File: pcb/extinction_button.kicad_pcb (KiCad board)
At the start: 2 copper layers, 47.8 x 61.3 mm, 36 parts, among them J1 DX07S016JA1R1500, J2 Conn_01x02, J3 Conn_01x06, SW1 R-667843, U1 ATmega32U4-A, U2 MIC5219-5.0YM5, Y1 ECS-160-10-36-CKM-TR3

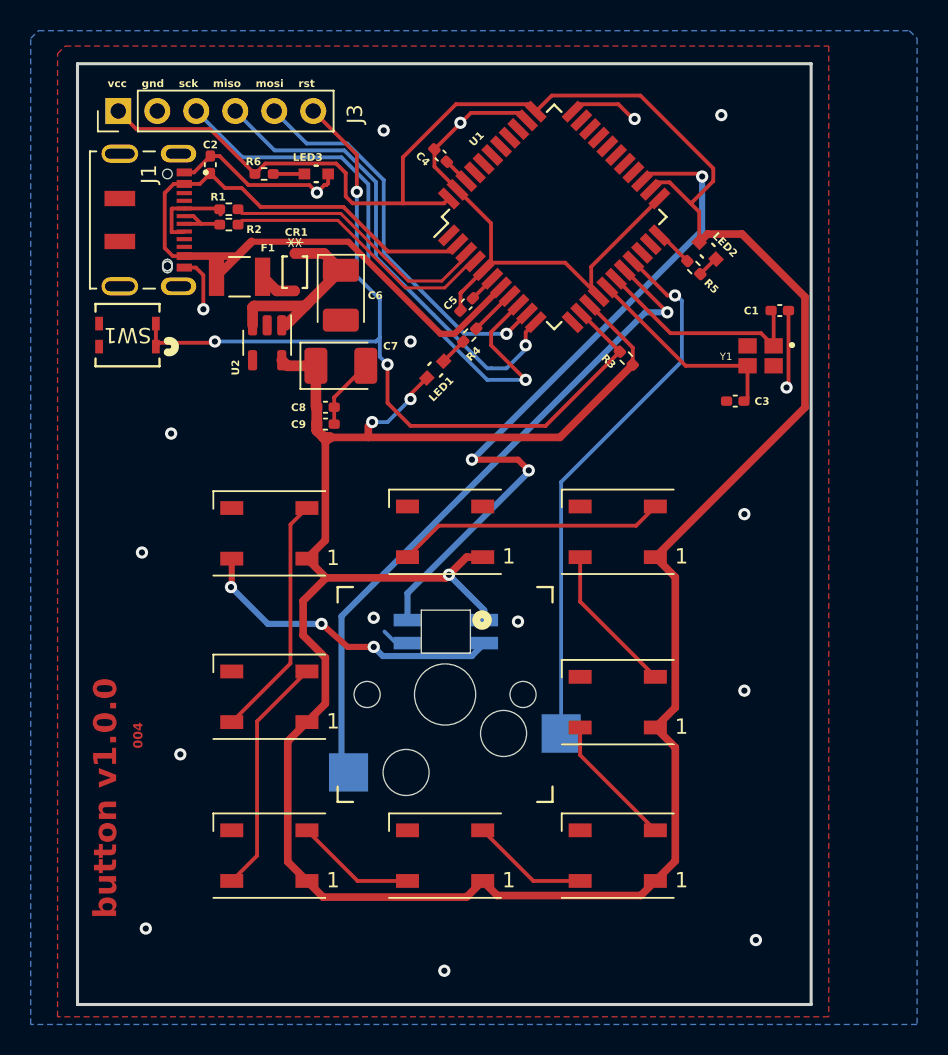
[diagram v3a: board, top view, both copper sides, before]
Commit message: re-add mounting holes
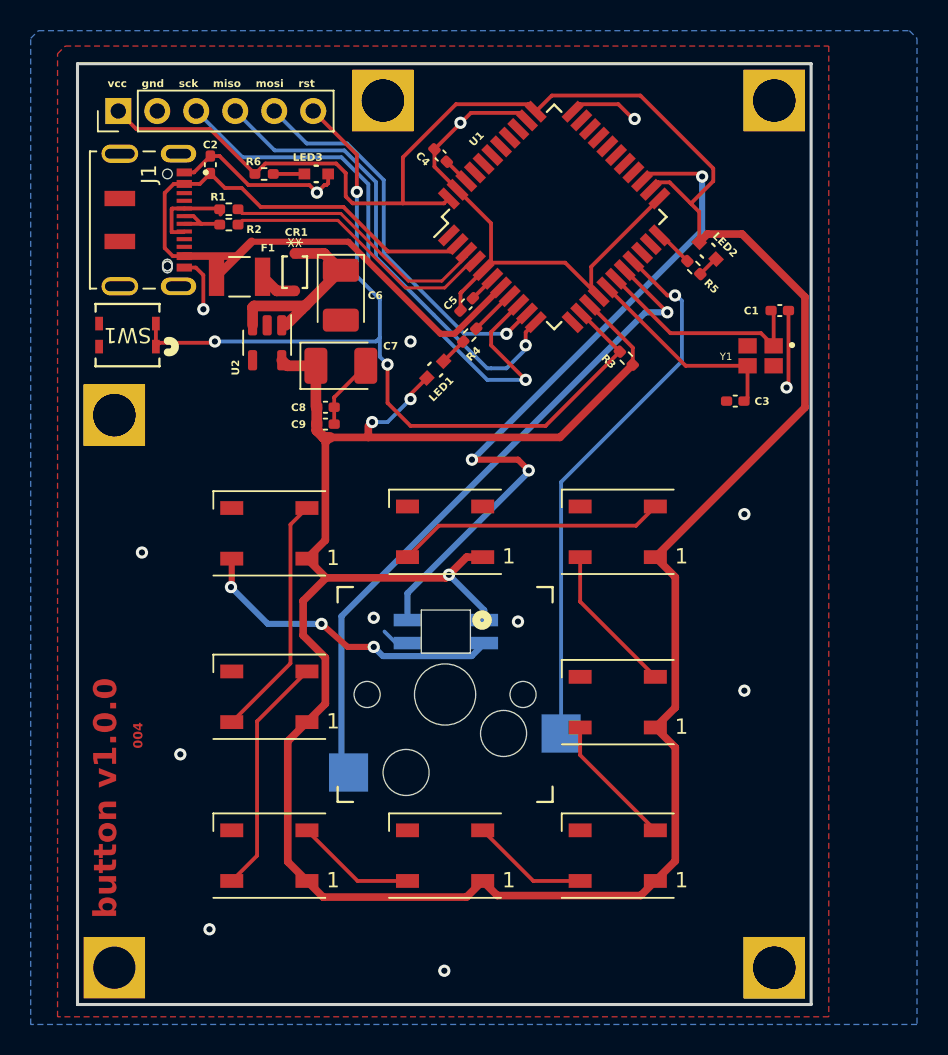
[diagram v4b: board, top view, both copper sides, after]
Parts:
- added ?: , , F.Cu at (196.2, 49.3)
- added ?: , clipboard:4f5b61f9-1e4c-4a2e-b6b5-7684ae1e77c1, F.Cu at (221.7, 105.8)
- added ?: , , F.Cu at (178.7, 69.8)
- added ?: , , F.Cu at (221.7, 49.3)
- added ?: , clipboard:4f5b61f9-1e4c-4a2e-b6b5-7684ae1e77c1, F.Cu at (196.2, 49.3)
- added ?: , clipboard:4f5b61f9-1e4c-4a2e-b6b5-7684ae1e77c1, F.Cu at (178.7, 69.8)
- added ?: , , F.Cu at (221.7, 105.8)
- added ?: , clipboard:4f5b61f9-1e4c-4a2e-b6b5-7684ae1e77c1, F.Cu at (178.7, 105.8)
- added ?: , clipboard:4f5b61f9-1e4c-4a2e-b6b5-7684ae1e77c1, F.Cu at (221.7, 49.3)
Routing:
- net GND: vias 18 -> 14
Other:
- board text removed: "JLCJLCJLCJLC"
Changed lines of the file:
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@@
     )
   )
+  (footprint "" (layer "F.Cu")
+    (at 196.2 49.3)
+    (fp_text reference "" (at 0 0) (layer "F.SilkS")
+        (effects (font (size 1.27 1.27) (thickness 0.15)))
+    )
+    (fp_text value "" (at 0 0) (layer "F.SilkS")
+        (effects (font (size 1.27 1.27) (thickness 0.15)))
+    )
+    (pad "1" thru_hole rect (at 0 0) (size 4 4) (drill 2.75) (layers "*.Cu" "*.Mask")
+      (net 1 "GND"))
+  )
   (footprint "Capacitor_SMD:C_0402_1005Metric_Pad0.74x0.62mm_HandSolder" (layer "F.Cu")
     (at 192.45706 69.283704)
@@
     )
   )
+  (footprint "clipboard:4f5b61f9-1e4c-4a2e-b6b5-7684ae1e77c1" (layer "F.Cu")
+    (at 221.7 105.8)
+    (fp_text reference "" (at 0 0) (layer "F.SilkS")
+        (effects (font (size 1.27 1.27) (thickness 0.15)))
+    )
+    (fp_text value "" (at 0 0) (layer "F.SilkS")
+        (effects (font (size 1.27 1.27) (thickness 0.15)))
+    )
+    (pad "1" thru_hole rect (at 0 0) (size 4 4) (drill 2.75) (layers "*.Cu" "*.Mask")
+      (net 1 "GND"))
+  )
   (footprint "Capacitor_Tantalum_SMD:CP_EIA-3528-15_AVX-H_Pad1.50x2.35mm_HandSolder" (layer "F.Cu")
     (at 193.45706 66.583704)
@@
     )
   )
+  (footprint "" (layer "F.Cu")
+    (at 178.7 69.8)
+    (fp_text reference "" (at 0 0) (layer "F.SilkS")
+        (effects (font (size 1.27 1.27) (thickness 0.15)))
+    )
+    (fp_text value "" (at 0 0) (layer "F.SilkS")
+        (effects (font (size 1.27 1.27) (thickness 0.15)))
+    )
+    (pad "1" thru_hole rect (at 0 0) (size 4 4) (drill 2.75) (layers "*.Cu" "*.Mask")
+      (net 1 "GND"))
+  )
   (footprint "LED_SMD:LED_WS2812B_PLCC4_5.0x5.0mm_P3.2mm" (layer "F.Cu")
     (at 211.5 77.4 180)
@@
     )
   )
+  (footprint "" (layer "F.Cu")
+    (at 221.7 49.3)
+    (fp_text reference "" (at 0 0) (layer "F.SilkS")
+        (effects (font (size 1.27 1.27) (thickness 0.15)))
+    )
+    (fp_text value "" (at 0 0) (layer "F.SilkS")
+        (effects (font (size 1.27 1.27) (thickness 0.15)))
+    )
+    (pad "1" thru_hole rect (at 0 0) (size 4 4) (drill 2.75) (layers "*.Cu" "*.Mask")
+      (net 1 "GND"))
+  )
   (footprint "Resistor_SMD:R_0402_1005Metric_Pad0.72x0.64mm_HandSolder" (layer "F.Cu")
     (at 188.45706 54.083704)
@@
     )
   )
+  (footprint "clipboard:4f5b61f9-1e4c-4a2e-b6b5-7684ae1e77c1" (layer "F.Cu")
+    (at 196.2 49.3)
+    (fp_text reference "" (at 0 0) (layer "F.SilkS")
+        (effects (font (size 1.27 1.27) (thickness 0.15)))
+    )
+    (fp_text value "" (at 0 0) (layer "F.SilkS")
+        (effects (font (size 1.27 1.27) (thickness 0.15)))
+    )
+    (pad "1" thru_hole rect (at 0 0) (size 4 4) (drill 2.75) (layers "*.Cu" "*.Mask")
+      (net 1 "GND"))
+  )
   (footprint "Connector_PinHeader_2.54mm:PinHeader_1x06_P2.54mm_Vertical" (layer "F.Cu")
     (at 178.95706 49.983704 90)
@@
     (property "ki_keywords" "connector")
     (attr through_hole)
-    (fp_text reference "J3" (at -0.2 15.42 90) (layer "F.SilkS")
+    (fp_text reference "J3" (at -0.2 15.42 90) (layer "F.SilkS") hide
         (effects (font (size 1 1) (thickness 0.15)))
     )
@@
     )
   )
+  (footprint "clipboard:4f5b61f9-1e4c-4a2e-b6b5-7684ae1e77c1" (layer "F.Cu")
+    (at 178.7 69.8)
+    (fp_text reference "" (at 0 0) (layer "F.SilkS")
+        (effects (font (size 1.27 1.27) (thickness 0.15)))
+    )
+    (fp_text value "" (at 0 0) (layer "F.SilkS")
+        (effects (font (size 1.27 1.27) (thickness 0.15)))
+    )
+    (pad "1" thru_hole rect (at 0 0) (size 4 4) (drill 2.75) (layers "*.Cu" "*.Mask")
+      (net 1 "GND"))
+  )
   (footprint "footprints:LED_LTST-C191KRKT_LTO" (layer "F.Cu")
     (at 191.85706 54.083704 180)
@@
     )
   )
+  (footprint "" (layer "F.Cu")
+    (at 221.7 105.8)
+    (fp_text reference "" (at 0 0) (layer "F.SilkS")
+        (effects (font (size 1.27 1.27) (thickness 0.15)))
+    )
+    (fp_text value "" (at 0 0) (layer "F.SilkS")
+        (effects (font (size 1.27 1.27) (thickness 0.15)))
+    )
+    (pad "1" thru_hole rect (at 0 0) (size 4 4) (drill 2.75) (layers "*.Cu" "*.Mask")
+      (net 1 "GND"))
+  )
+  (footprint "clipboard:4f5b61f9-1e4c-4a2e-b6b5-7684ae1e77c1" (layer "F.Cu")
+    (at 178.7 105.8)
+    (fp_text reference "" (at 0 0) (layer "F.SilkS")
+        (effects (font (size 1.27 1.27) (thickness 0.15)))
+    )
+    (fp_text value "" (at 0 0) (layer "F.SilkS")
+        (effects (font (size 1.27 1.27) (thickness 0.15)))
+    )
+    (pad "1" thru_hole rect (at 0 0) (size 4 4) (drill 2.75) (layers "*.Cu" "*.Mask")
+      (net 1 "GND"))
+  )
   (footprint "ECS-160-10-36-CKM-TR3:XTAL_ECS-160-10-36-CKM-TR3" (layer "F.Cu")
     (at 220.80706 65.933704 180)
@@
     )
   )
+  (footprint "clipboard:4f5b61f9-1e4c-4a2e-b6b5-7684ae1e77c1" (layer "F.Cu")
+    (at 221.7 49.3)
+    (fp_text reference "" (at 0 0) (layer "F.SilkS")
+        (effects (font (size 1.27 1.27) (thickness 0.15)))
+    )
+    (fp_text value "" (at 0 0) (layer "F.SilkS")
+        (effects (font (size 1.27 1.27) (thickness 0.15)))
+    )
+    (pad "1" thru_hole rect (at 0 0) (size 4 4) (drill 2.75) (layers "*.Cu" "*.Mask")
+      (net 1 "GND"))
+  )
   (footprint "Package_QFP:TQFP-44_10x10mm_P0.8mm" (layer "F.Cu")
     (at 207.35706 56.883704 45)
@@
     )
   )
-  (gr_text "JLCJLCJLCJLC" (at 178.9 102.5 90) (layer "B.SilkS")
-    (effects (font (size 0.8 0.8) (thickness 0.15) bold) (justify left bottom))
-  )
   (gr_text "vcc    gnd    sck    miso    mosi    rst" (at 178.25706 48.483704) (layer "F.SilkS")
     (effects (font (size 0.5 0.5) (thickness 0.1) bold) (justify left bottom))
@@
   (segment (start 201.931843 50.106355) (end 205.105194 50.106355) (width 0.25) (layer "F.Cu") (net 1))
   (segment (start 192.514262 54.806802) (end 192.393198 54.806802) (width 0.25) (layer "F.Cu") (net 1))
-  (via (at 180.75 103.25) (size 0.8) (drill 0.4) (layers "F.Cu" "B.Cu") (free) (net 1))
+  (via (at 184.9 103.3) (size 0.8) (drill 0.4) (layers "F.Cu" "B.Cu") (free) (net 1))
   (via (at 205 83.25) (size 0.8) (drill 0.4) (layers "F.Cu" "B.Cu") (free) (net 1))
-  (via (at 220.5 104) (size 0.8) (drill 0.4) (layers "F.Cu" "B.Cu") (free) (net 1))
   (via (at 198 65) (size 0.8) (drill 0.4) (layers "F.Cu" "B.Cu") (free) (net 1))
-  (via (at 218.25 50.25) (size 0.8) (drill 0.4) (layers "F.Cu" "B.Cu") (free) (net 1))
   (via (at 201.25 50.75) (size 0.8) (drill 0.4) (layers "F.Cu" "B.Cu") (net 1))
   (via (at 195.6 83) (size 0.8) (drill 0.4) (layers "F.Cu" "B.Cu") (free) (net 1))
@@
   (via (at 212.6 50.5) (size 0.8) (drill 0.4) (layers "F.Cu" "B.Cu") (net 1))
   (via (at 222.5 68) (size 0.8) (drill 0.4) (layers "F.Cu" "B.Cu") (free) (net 1))
-  (via (at 196.25 51.25) (size 0.8) (drill 0.4) (layers "F.Cu" "B.Cu") (free) (net 1))
-  (via (at 182.4 71) (size 0.8) (drill 0.4) (layers "F.Cu" "B.Cu") (free) (net 1))
   (via (at 219.75 87.75) (size 0.8) (drill 0.4) (layers "F.Cu" "B.Cu") (free) (net 1))
   (via (at 200.2 106) (size 0.8) (drill 0.4) (layers "F.Cu" "B.Cu") (free) (net 1))

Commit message: enshittify board
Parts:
- added G***: LOGO, LOGO, F.Cu at (180.1, 99.4)
- added G***: LOGO, LOGO, B.Cu at (220.0, 96.2)
- added G***: LOGO, LOGO, B.Cu at (207.4, 56.9)
- moved LED4 9.00 mm to (200.4, 92.9), turned to 0 degrees
- turned J2 to 0 degrees
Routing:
- net D3: track 43.7 -> 28.0 mm
- net D4: track 46.1 -> 58.6 mm
- net Net-(D7-DIN): track 20.9 -> 25.4 mm
- net D2: track 35.9 -> 40.3 mm, vias 1 -> 3
- net VCC: track 229.0 -> 233.2 mm
- net GND: track 68.4 -> 66.6 mm, vias 14 -> 17
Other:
- board text added: "005"
- board text added: "8883774855"
- board text added: ":~)"
- board text added: "i am in your walls"
- board text removed: "004"
